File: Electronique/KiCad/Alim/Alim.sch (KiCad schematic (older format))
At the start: 18 parts, among them P1 CONN_2, P2 CONN_2, P3 CONN_2, T1 MMBT2907A, T2 MMBT2907A, T3 NJVMJD44H11, T4 NJVMJD44H11

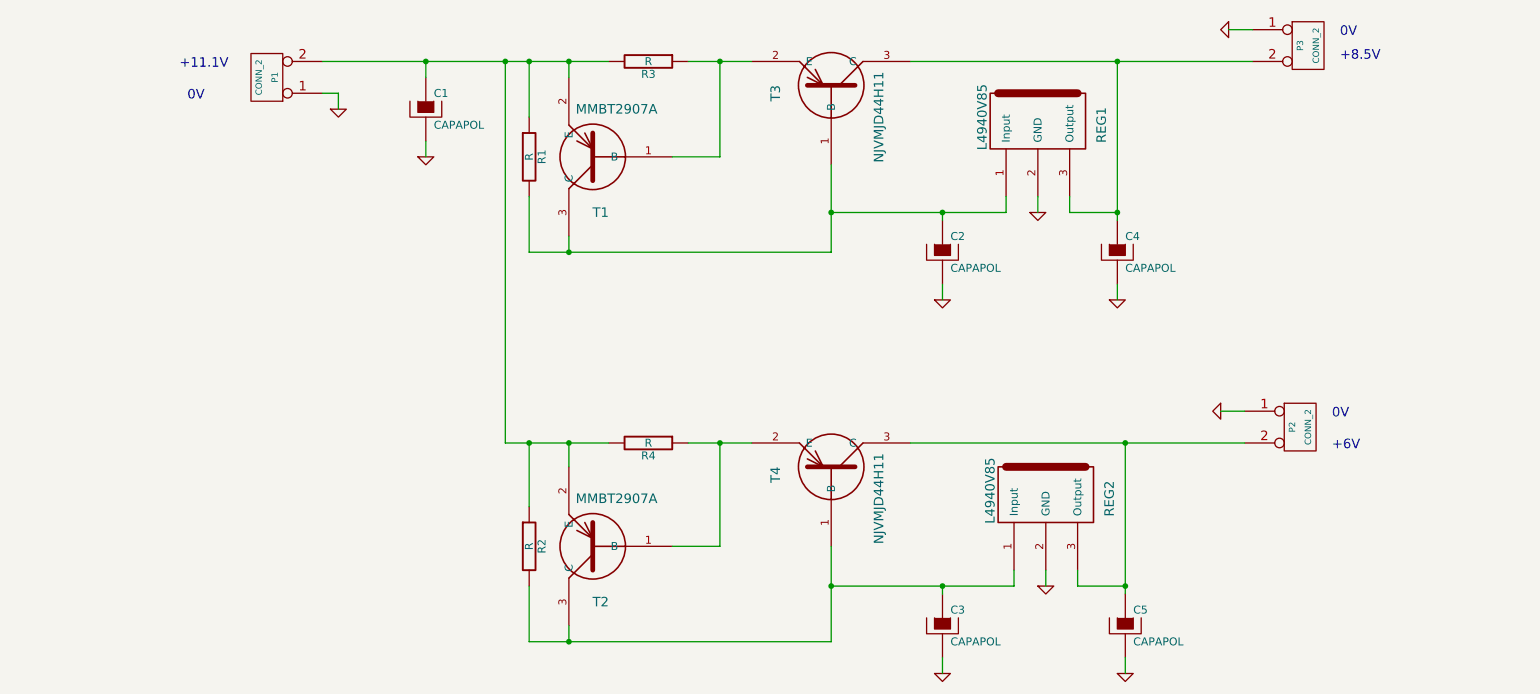
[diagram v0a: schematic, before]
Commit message: Ajout de quelques fichiers et mise à jour des document. Ajout de la netlist (incomplète).
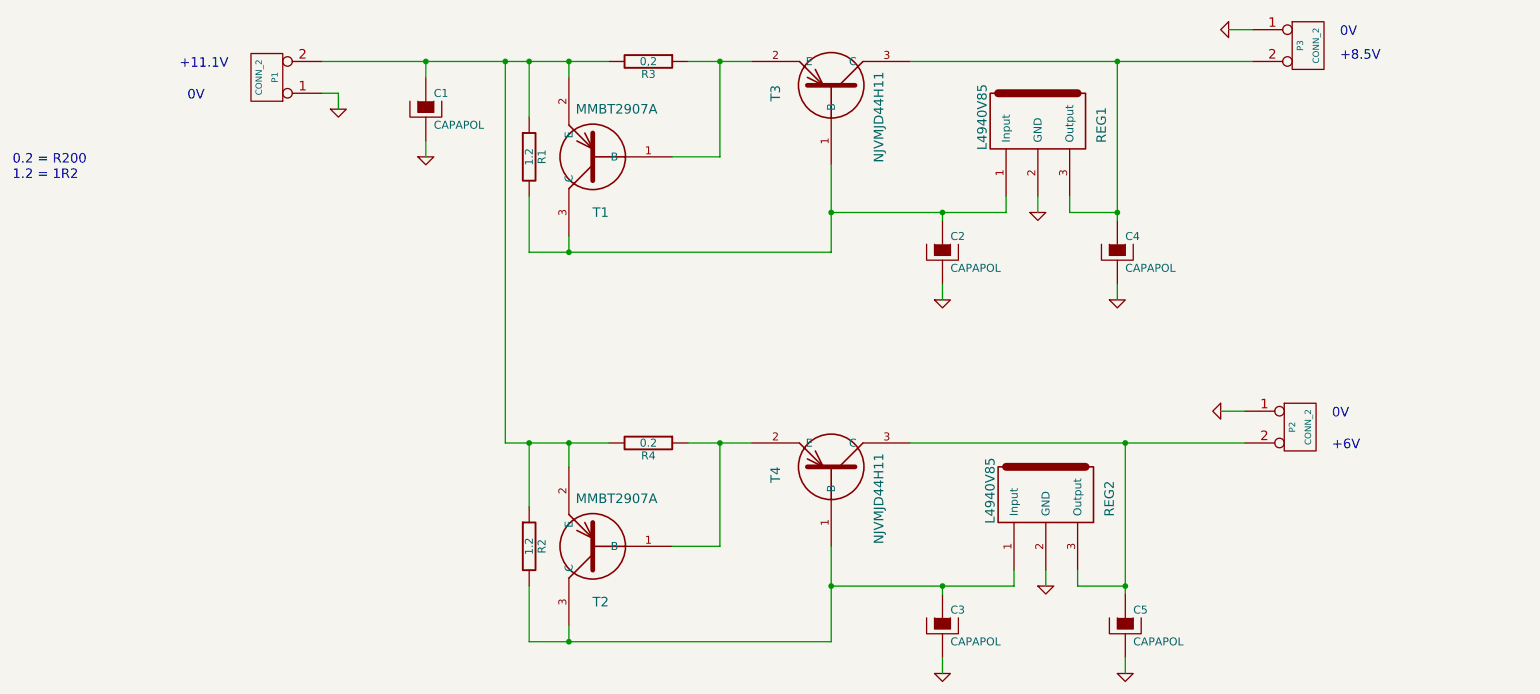
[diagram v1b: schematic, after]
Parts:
- R1, R2: value R -> 1.2
- R3: value R -> 0,2
- R4: value R -> 0.2
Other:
- note added: "0.2 = R200\n1.2 = 1R2"
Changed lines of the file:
@@
-EESchema Schematic File Version 2  date mar. 23 sept. 2014 12:43:10 CEST
+EESchema Schematic File Version 2  date ven. 26 sept. 2014 15:28:32 CEST
 LIBS:power
 LIBS:device
@@
 Sheet 1 1
 Title ""
-Date "23 sep 2014"
+Date "26 sep 2014"
 Rev ""
 Comp ""
@@
 Comment4 ""
 $EndDescr
+Text Notes 950  2450 0    60   ~ 0
+0.2 = R200\n1.2 = 1R2
 Text Notes 9250 4150 0    60   ~ 0
 +6V
@@
 P 4950 4100
 F 0 "R4" V 5030 4100 50  0000 C CNN
-F 1 "R" V 4950 4100 50  0000 C CNN
+F 1 "0.2" V 4950 4100 50  0000 C CNN
 	1    4950 4100
 	0    1    1    0
@@
 P 4950 1700
 F 0 "R3" V 5030 1700 50  0000 C CNN
-F 1 "R" V 4950 1700 50  0000 C CNN
+F 1 "0,2" V 4950 1700 50  0000 C CNN
 	1    4950 1700
 	0    1    1    0
@@
 P 4200 4750
 F 0 "R2" V 4280 4750 50  0000 C CNN
-F 1 "R" V 4200 4750 50  0000 C CNN
+F 1 "1.2" V 4200 4750 50  0000 C CNN
 	1    4200 4750
 	1    0    0    -1
@@
 P 4200 2300
 F 0 "R1" V 4280 2300 50  0000 C CNN
-F 1 "R" V 4200 2300 50  0000 C CNN
+F 1 "1.2" V 4200 2300 50  0000 C CNN
 	1    4200 2300
 	1    0    0    -1

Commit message: Modification du Circuit. En raison d'une modification future, la version en cours est incorrecte. Veuillez noter que ce commit en l'état est pour mémoire avant toute nouvelle version de PCB.
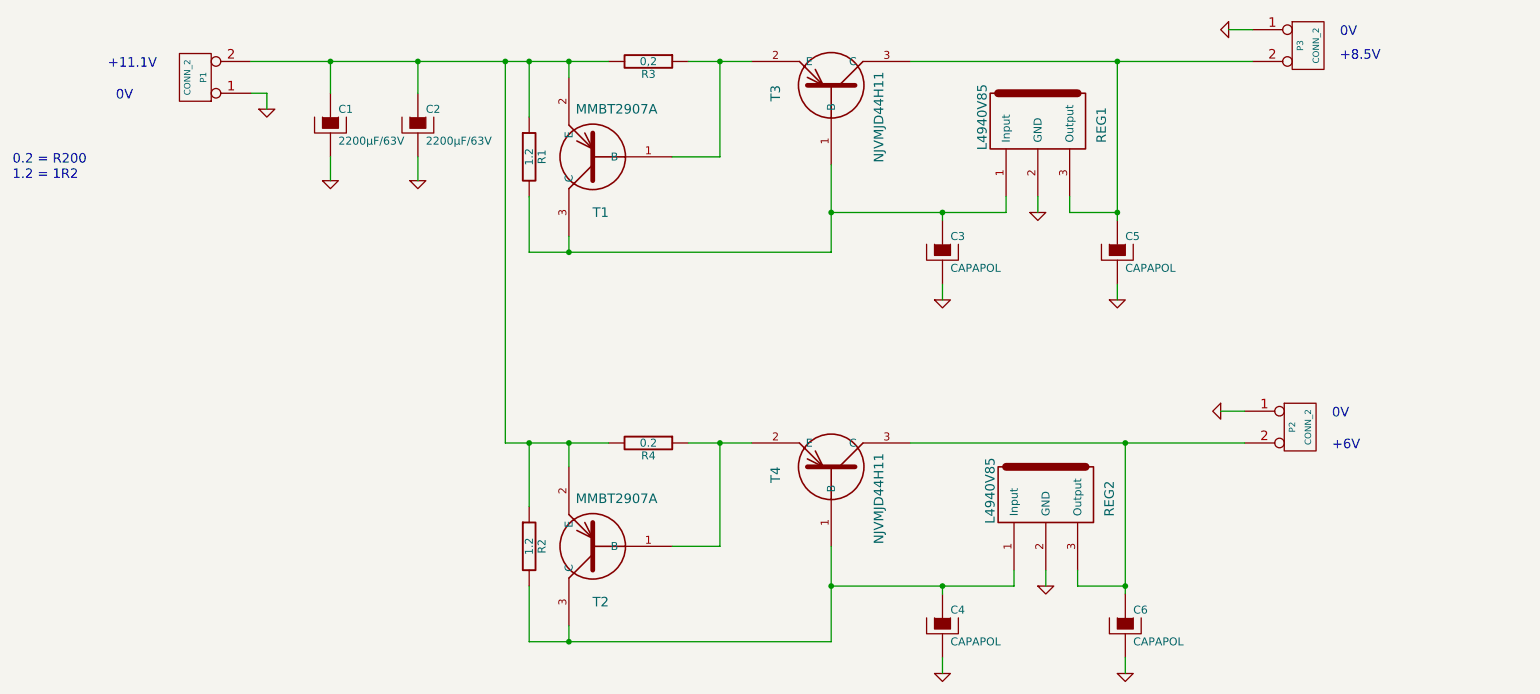
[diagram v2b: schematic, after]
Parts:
- added C1: 2200µF/63V, symbol CAPAPOL
- C2: renamed from C1; value CAPAPOL -> 2200µF/63V
- renumbered C2 to C3, C3 to C4, C4 to C5, C5 to C6
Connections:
- net GND: now also C1.2
- net at C2.1, P1.2 (PM), R1.1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: now also C1.1
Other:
- moved on the sheet: C2, P1
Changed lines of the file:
@@
-EESchema Schematic File Version 2  date ven. 26 sept. 2014 15:28:32 CEST
+EESchema Schematic File Version 2  date sam. 27 sept. 2014 09:30:36 CEST
 LIBS:power
 LIBS:device
@@
 Sheet 1 1
 Title ""
-Date "26 sep 2014"
+Date "27 sep 2014"
 Rev ""
 Comp ""
@@
 Comment4 ""
 $EndDescr
+Wire Wire Line
+	3500 2300 3500 2450
+Connection ~ 3500 1700
+Wire Wire Line
+	3500 1900 3500 1700
+Wire Wire Line
+	2550 2000 2550 1900
+Wire Wire Line
+	2550 1900 2450 1900
+Wire Wire Line
+	8700 4100 6600 4100
+Wire Wire Line
+	8750 1700 6600 1700
+Wire Wire Line
+	6800 5550 6800 5450
+Connection ~ 6100 5000
+Wire Wire Line
+	6100 5000 7250 5000
+Wire Wire Line
+	7250 5000 7250 4900
+Connection ~ 7950 5000
+Wire Wire Line
+	7950 5000 7650 5000
+Wire Wire Line
+	7650 5000 7650 4900
+Wire Wire Line
+	7950 5550 7950 5450
+Connection ~ 7950 4100
+Connection ~ 4450 5350
+Wire Wire Line
+	4450 5250 4450 5350
+Wire Wire Line
+	5200 4100 5600 4100
+Connection ~ 4450 4100
+Wire Wire Line
+	4450 4100 4450 4250
+Connection ~ 4050 1700
+Wire Wire Line
+	4700 4100 4050 4100
+Wire Wire Line
+	4050 4100 4050 1700
+Wire Wire Line
+	6800 3200 6800 3100
+Wire Wire Line
+	6800 2650 6800 2700
+Wire Wire Line
+	7200 2550 7200 2650
+Connection ~ 7900 2650
+Wire Wire Line
+	7900 2650 7600 2650
+Wire Wire Line
+	7600 2650 7600 2550
+Connection ~ 7900 1700
+Connection ~ 5400 1700
+Wire Wire Line
+	5100 2300 5400 2300
+Wire Wire Line
+	5400 2300 5400 1700
+Connection ~ 4450 2900
+Wire Wire Line
+	4450 2800 4450 2900
+Connection ~ 4200 1700
+Wire Wire Line
+	4200 2050 4200 1700
+Connection ~ 4450 1700
+Wire Wire Line
+	4450 1800 4450 1700
+Wire Wire Line
+	4200 2550 4200 2900
+Wire Wire Line
+	4200 2900 6100 2900
+Wire Wire Line
+	6100 2900 6100 2350
+Wire Wire Line
+	5200 1700 5600 1700
+Wire Wire Line
+	7900 1700 7900 2700
+Wire Wire Line
+	7400 2650 7400 2550
+Wire Wire Line
+	7200 2650 6100 2650
+Connection ~ 6100 2650
+Connection ~ 6800 2650
+Wire Wire Line
+	7900 3200 7900 3100
+Wire Wire Line
+	4200 4100 4200 4500
+Connection ~ 4200 4100
+Wire Wire Line
+	4200 5000 4200 5350
+Wire Wire Line
+	4200 5350 6100 5350
+Wire Wire Line
+	6100 5350 6100 4750
+Wire Wire Line
+	5400 4100 5400 4750
+Wire Wire Line
+	5400 4750 5100 4750
+Connection ~ 5400 4100
+Wire Wire Line
+	7950 4100 7950 5050
+Wire Wire Line
+	7450 4900 7450 5000
+Wire Wire Line
+	6800 5050 6800 5000
+Connection ~ 6800 5000
+Wire Wire Line
+	8750 1500 8600 1500
+Wire Wire Line
+	8700 3900 8550 3900
+Wire Wire Line
+	2450 1700 4700 1700
+Wire Wire Line
+	2950 1900 2950 1700
+Connection ~ 2950 1700
+Wire Wire Line
+	2950 2300 2950 2450
+$Comp
+L GND #PWR01
+U 1 1 5426672A
+P 2950 2450
+F 0 "#PWR01" H 2950 2450 30  0001 C CNN
+F 1 "GND" H 2950 2380 30  0001 C CNN
+	1    2950 2450
+	1    0    0    -1
+$EndComp
+$Comp
+L CAPAPOL C1
+U 1 1 54266710
+P 2950 2100
+F 0 "C1" H 3000 2200 50  0000 L CNN
+F 1 "2200µF/63V" H 3000 2000 50  0000 L CNN
+	1    2950 2100
+	1    0    0    -1
+$EndComp
+$Comp
+L CAPAPOL C2
+U 1 1 542148DF
+P 3500 2100
+F 0 "C2" H 3550 2200 50  0000 L CNN
+F 1 "2200µF/63V" H 3550 2000 50  0000 L CNN
+	1    3500 2100
+	1    0    0    -1
+$EndComp
 Text Notes 950  2450 0    60   ~ 0
 0.2 = R200\n1.2 = 1R2
@@
 Text Notes 9250 3950 0    60   ~ 0
 0V
-Wire Wire Line
-	8700 4100 6600 4100
-Wire Wire Line
-	8750 1700 6600 1700
-Wire Wire Line
-	6800 5550 6800 5450
-Connection ~ 6100 5000
-Wire Wire Line
-	6100 5000 7250 5000
-Wire Wire Line
-	7250 5000 7250 4900
-Connection ~ 7950 5000
-Wire Wire Line
-	7950 5000 7650 5000
-Wire Wire Line
-	7650 5000 7650 4900
-Wire Wire Line
-	7950 5550 7950 5450
-Connection ~ 7950 4100
-Connection ~ 4450 5350
-Wire Wire Line
-	4450 5250 4450 5350
-Wire Wire Line
-	5200 4100 5600 4100
-Connection ~ 4450 4100
-Wire Wire Line
-	4450 4100 4450 4250
-Connection ~ 4050 1700
-Wire Wire Line
-	4700 4100 4050 4100
-Wire Wire Line
-	4050 4100 4050 1700
-Wire Wire Line
-	6800 3200 6800 3100
-Wire Wire Line
-	6800 2650 6800 2700
-Wire Wire Line
-	7200 2550 7200 2650
-Connection ~ 7900 2650
-Wire Wire Line
-	7900 2650 7600 2650
-Wire Wire Line
-	7600 2650 7600 2550
-Connection ~ 7900 1700
-Connection ~ 5400 1700
-Wire Wire Line
-	5100 2300 5400 2300
-Wire Wire Line
-	5400 2300 5400 1700
-Connection ~ 4450 2900
-Wire Wire Line
-	4450 2800 4450 2900
-Connection ~ 4200 1700
-Wire Wire Line
-	4200 2050 4200 1700
-Wire Wire Line
-	3000 2000 3000 1900
-Wire Wire Line
-	3000 1900 2900 1900
-Connection ~ 4450 1700
-Wire Wire Line
-	4450 1800 4450 1700
-Wire Wire Line
-	2900 1700 4700 1700
-Wire Wire Line
-	3550 1800 3550 1700
-Connection ~ 3550 1700
-Wire Wire Line
-	3550 2200 3550 2300
-Wire Wire Line
-	4200 2550 4200 2900
-Wire Wire Line
-	4200 2900 6100 2900
-Wire Wire Line
-	6100 2900 6100 2350
-Wire Wire Line
-	5200 1700 5600 1700
-Wire Wire Line
-	7900 1700 7900 2700
-Wire Wire Line
-	7400 2650 7400 2550
-Wire Wire Line
-	7200 2650 6100 2650
-Connection ~ 6100 2650
-Connection ~ 6800 2650
-Wire Wire Line
-	7900 3200 7900 3100
-Wire Wire Line
-	4200 4100 4200 4500
-Connection ~ 4200 4100
-Wire Wire Line
-	4200 5000 4200 5350
-Wire Wire Line
-	4200 5350 6100 5350
-Wire Wire Line
-	6100 5350 6100 4750
-Wire Wire Line
-	5400 4100 5400 4750
-Wire Wire Line
-	5400 4750 5100 4750
-Connection ~ 5400 4100
-Wire Wire Line
-	7950 4100 7950 5050
-Wire Wire Line
-	7450 4900 7450 5000
-Wire Wire Line
-	6800 5050 6800 5000
-Connection ~ 6800 5000
-Wire Wire Line
-	8750 1500 8600 1500
-Wire Wire Line
-	8700 3900 8550 3900
 Text Notes 9300 1550 0    60   ~ 0
 0V
 Text Notes 9300 1700 0    60   ~ 0
 +8.5V
-Text Notes 2050 1950 0    60   ~ 0
+Text Notes 1600 1950 0    60   ~ 0
 0V
-Text Notes 2000 1750 0    60   ~ 0
+Text Notes 1550 1750 0    60   ~ 0
 +11.1V
 $Comp
-L GND #PWR4
+L GND #PWR02
 U 1 1 542149E6
 P 6800 5550
-F 0 "#PWR4" H 6800 5550 30  0001 C CNN
+F 0 "#PWR02" H 6800 5550 30  0001 C CNN
 F 1 "GND" H 6800 5480 30  0001 C CNN
 	1    6800 5550
@@
 $EndComp
 $Comp
-L GND #PWR8
+L GND #PWR03
 U 1 1 542149E4
 P 7950 5550
-F 0 "#PWR8" H 7950 5550 30  0001 C CNN
+F 0 "#PWR03" H 7950 5550 30  0001 C CNN
 F 1 "GND" H 7950 5480 30  0001 C CNN
 	1    7950 5550
@@
 $EndComp
 $Comp
-L GND #PWR6
+L GND #PWR04
 U 1 1 542149E1
 P 7450 5000
-F 0 "#PWR6" H 7450 5000 30  0001 C CNN
+F 0 "#PWR04" H 7450 5000 30  0001 C CNN
 F 1 "GND" H 7450 4930 30  0001 C CNN
 	1    7450 5000
@@
 $EndComp
 $Comp
-L GND #PWR9
+L GND #PWR05
 U 1 1 542149DE
 P 8550 3900
-F 0 "#PWR9" H 8550 3900 30  0001 C CNN
+F 0 "#PWR05" H 8550 3900 30  0001 C CNN
 F 1 "GND" H 8550 3830 30  0001 C CNN
 	1    8550 3900
@@
 $EndComp
 $Comp
-L GND #PWR10
+L GND #PWR06
 U 1 1 542149DA
 P 8600 1500
-F 0 "#PWR10" H 8600 1500 30  0001 C CNN
+F 0 "#PWR06" H 8600 1500 30  0001 C CNN
 F 1 "GND" H 8600 1430 30  0001 C CNN
 	1    8600 1500
@@
 $EndComp
 $Comp
-L GND #PWR7
+L GND #PWR07
 U 1 1 542149D6
 P 7900 3200
-F 0 "#PWR7" H 7900 3200 30  0001 C CNN
+F 0 "#PWR07" H 7900 3200 30  0001 C CNN
 F 1 "GND" H 7900 3130 30  0001 C CNN
 	1    7900 3200
@@
 $EndComp
 $Comp
-L GND #PWR3
+L GND #PWR08
 U 1 1 542149D3
 P 6800 3200
-F 0 "#PWR3" H 6800 3200 30  0001 C CNN
+F 0 "#PWR08" H 6800 3200 30  0001 C CNN
 F 1 "GND" H 6800 3130 30  0001 C CNN
 	1    6800 3200
@@
 $EndComp
 $Comp
-L GND #PWR5
+L GND #PWR09
 U 1 1 542149CF
 P 7400 2650
-F 0 "#PWR5" H 7400 2650 30  0001 C CNN
+F 0 "#PWR09" H 7400 2650 30  0001 C CNN
 F 1 "GND" H 7400 2580 30  0001 C CNN
 	1    7400 2650
@@
 $EndComp
 $Comp
-L GND #PWR2
+L GND #PWR010
 U 1 1 542149CA
-P 3550 2300
-F 0 "#PWR2" H 3550 2300 30  0001 C CNN
-F 1 "GND" H 3550 2230 30  0001 C CNN
-	1    3550 2300
-	1    0    0    -1
-$EndComp
-$Comp
-L GND #PWR1
+P 3500 2450
+F 0 "#PWR010" H 3500 2450 30  0001 C CNN
+F 1 "GND" H 3500 2380 30  0001 C CNN
+	1    3500 2450
+	1    0    0    -1
+$EndComp
+$Comp
+L GND #PWR011
 U 1 1 542149C5
-P 3000 2000
-F 0 "#PWR1" H 3000 2000 30  0001 C CNN
-F 1 "GND" H 3000 1930 30  0001 C CNN
-	1    3000 2000
+P 2550 2000
+F 0 "#PWR011" H 2550 2000 30  0001 C CNN
+F 1 "GND" H 2550 1930 30  0001 C CNN
+	1    2550 2000
 	1    0    0    -1
 $EndComp
@@
 $EndComp
 $Comp
-L CAPAPOL C5
+L CAPAPOL C6
 U 1 1 54214981
 P 7950 5250
-F 0 "C5" H 8000 5350 50  0000 L CNN
+F 0 "C6" H 8000 5350 50  0000 L CNN
 F 1 "CAPAPOL" H 8000 5150 50  0000 L CNN
 	1    7950 5250
@@
 $EndComp
 $Comp
-L CAPAPOL C3
+L CAPAPOL C4
 U 1 1 5421497E
 P 6800 5250
-F 0 "C3" H 6850 5350 50  0000 L CNN
+F 0 "C4" H 6850 5350 50  0000 L CNN
 F 1 "CAPAPOL" H 6850 5150 50  0000 L CNN
 	1    6800 5250
@@
 $EndComp
 $Comp
-L CAPAPOL C4
+L CAPAPOL C5
 U 1 1 5421497B
 P 7900 2900
-F 0 "C4" H 7950 3000 50  0000 L CNN
+F 0 "C5" H 7950 3000 50  0000 L CNN
 F 1 "CAPAPOL" H 7950 2800 50  0000 L CNN
 	1    7900 2900
@@
 $EndComp
 $Comp
-L CAPAPOL C2
+L CAPAPOL C3
 U 1 1 54214975
 P 6800 2900
-F 0 "C2" H 6850 3000 50  0000 L CNN
+F 0 "C3" H 6850 3000 50  0000 L CNN
 F 1 "CAPAPOL" H 6850 2800 50  0000 L CNN
 	1    6800 2900
@@
 $EndComp
 $Comp
-L CAPAPOL C1
-U 1 1 542148DF
-P 3550 2000
-F 0 "C1" H 3600 2100 50  0000 L CNN
-F 1 "CAPAPOL" H 3600 1900 50  0000 L CNN
-	1    3550 2000
-	1    0    0    -1
-$EndComp
-$Comp
 L CONN_2 P1
 U 1 1 542148C0
-P 2550 1800
-F 0 "P1" V 2500 1800 40  0000 C CNN
-F 1 "CONN_2" V 2600 1800 40  0000 C CNN
-	1    2550 1800
+P 2100 1800
+F 0 "P1" V 2050 1800 40  0000 C CNN
+F 1 "CONN_2" V 2150 1800 40  0000 C CNN
+	1    2100 1800
 	-1   0    0    1
 $EndComp
